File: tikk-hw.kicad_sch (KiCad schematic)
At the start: 18 parts, among them P6 ZX-SH1.0-4PWT, SW1 TS24CA, SW2 TS24CA, U1 IS31FL3731-QFLS2-TR, U2 LIS2DH12TR, U3 ProMicro, U4 CP6208DTR(XBLW), U5 TMP102AIDRLR

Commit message: initial placements all finished
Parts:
- added J1: 51281-0598, 512810598, symbol easyeda2kicad:51281-0598
- added LED10, LED100, LED101, LED102, LED103, LED104, LED105, LED11, LED12, LED13, LED14, LED15, LED16, LED17, LED18, LED19, LED20, LED21, LED22, LED23, LED24, LED25, LED26, LED27, LED28, LED29, LED30, LED31, LED32, LED33, LED34, LED35, LED36, LED37, LED38, LED39, LED40, LED41, LED42, LED43, LED44, LED45, LED46, LED47, LED48, LED49, LED50, LED51, LED52, LED53, LED54, LED55, LED56, LED57, LED58, LED59, LED60, LED61, LED62, LED63, LED64, LED65, LED66, LED67, LED68, LED69, LED70, LED71, LED72, LED73, LED74, LED75, LED76, LED77, LED78, LED79, LED8, LED80, LED81, LED82, LED83, LED84, LED85, LED86, LED87, LED88, LED89, LED9, LED90, LED91, LED92, LED93, LED94, LED95, LED96, LED97, LED98, LED99: F.0402.00003/P2-0402R1TS2-045T-001, easyeda2kicad:LED0402-RD, symbol easyeda2kicad:F.0402.00003_P2-0402R1TS2-045T-001
- added R1, R2: 100K, Resistor_SMD:R_0402_1005Metric, symbol Device:R
- added TP1: NC1, TestPoint:TestPoint_Pad_1.0x1.0mm, symbol Connector:TestPoint
- added TP2: NFC1, TestPoint:TestPoint_Pad_1.0x1.0mm, symbol Connector:TestPoint
- added TP3: NC2, TestPoint:TestPoint_Pad_1.0x1.0mm, symbol Connector:TestPoint
- added TP4: NC3, TestPoint:TestPoint_Pad_1.0x1.0mm, symbol Connector:TestPoint
- added TP5: NFC2, TestPoint:TestPoint_Pad_1.0x1.0mm, symbol Connector:TestPoint
- added TP6: SWCLK, TestPoint:TestPoint_THTPad_1.0x1.0mm_Drill0.5mm, symbol Connector:TestPoint
- added TP7: SWDIO, TestPoint:TestPoint_THTPad_1.0x1.0mm_Drill0.5mm, symbol Connector:TestPoint
- added U6: CP6208DTR(XBLW), easyeda2kicad:SOP-8_L4.9-W3.9-P1.27-LS6.0-BL, symbol easyeda2kicad:CP6208DTR(XBLW)
- U3: value ProMicro -> Tenstar nRF52840; footprint nrfmicro:pro_micro -> nrfmicro:tenstar_nrf52840
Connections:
- net P0.03 is gone; now on net P1.11: U3.10 (1.11)
- net P0.15 is gone; now on net MOTOR2-A: U3.17 (0.17)
- net P0.17 is gone; now on net MOTOR2-B: U3.18 (0.20)
- net P0.28 is gone; now on net P0.10: U3.11 (0.10)
- net P0.31 is gone; now on net P0.29: U3.6 (0.29)
- net P1.06 is gone; now on net SDA: U3.24 (1.06)
- net EXT_VCC: now also U5.5 (V+)
- net GND: now also SW1.3, U5.2 (GND), U5.4 (ADD0), J1.6 (MP1), J1.7 (MP2), R2.2
- net P0.02: now also U3.7 (0.02); no longer U3.8 (PF7)
- net P0.09: now also U3.12 (0.09), J1.5, TP5.1; no longer U3.22 (PE6)
- net P0.10: now also J1.2, TP2.1; no longer U3.23 (PB4)
- net P0.13: now also U3.22 (0.11); no longer U3.20 (PC6)
- net P0.24: now also U3.20 (0.24); no longer U3.21 (PD7)
- net P0.29: no longer U3.7 (PF6)
- net P1.11: no longer U3.12 (PB6)
- net RESET: now also SW1.4
- net VBAT: now also R1.1
- net at U4.2 (Bout): now also H3.3
- net at U4.3 (Aout): now also H3.4
- net MOTOR2-B: now reaches U4.5 (Bin)
- net MOTOR2-A: now reaches U4.8 (Ain)
- net at H3.1: now also U6.2 (Bout)
- net at H3.2: now also U6.3 (Aout)
- net SCL: now reaches U5.1 (SCL)
- net SCL: now also U3.23 (1.04)
- net TMP102_ALERT: now reaches U5.3 (ALERT)
- net SDA: now reaches U5.6 (SDA)
- net P0.06 renamed MOTOR1-A
- net MOTOR1-A: now also U6.8 (Ain)
- net P0.08 renamed MOTOR1-B
- net MOTOR1-B: now also U6.5 (Bin)
- net P0.20 renamed P0.22
- net P0.30 renamed BATTERY-V
- net BATTERY-V: now also R1.2, R2.1
- new net: J1.4, TP4.1
- new net: J1.1, TP1.1
- new net: J1.3, TP3.1
- new net P1.00: U3.21 (1.00)
- new net P1.15: U3.8 (1.15)
- no-connect marks 0 -> 2
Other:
- note added: "Passthrough for programming pads on the tenstar board"
- moved on the sheet: H1, H2, H3, LED1, LED2, LED3, LED4, LED5, LED6, LED7, P6, SW1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

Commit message: added caps
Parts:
- added C10, C11, C12, C8, C9: CC0402KRX7R7BB104, easyeda2kicad:C0402, symbol easyeda2kicad:CC0402KRX7R7BB104
- added C13, C14: CC0603JRNPO8BN561, easyeda2kicad:C0603, symbol easyeda2kicad:CC0603JRNPO8BN561
- added C2: CL21A106KAYNNNE, easyeda2kicad:C0805, symbol easyeda2kicad:CL21A106KAYNNNE
- added C4, C5, C6, C7: CL31A107MQHNNNE, easyeda2kicad:C1206, symbol easyeda2kicad:CL31A107MQHNNNE
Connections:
- net GND: now also SW2.3, C12.1, C13.1, C14.1, C2.1, C4.1, C5.1, C6.1, C7.1, C8.1, C9.1
- net RESET: now also SW2.4
- net at U6.1 (Vcc): now also C4.2, C7.2, C8.2
- net at U6.2 (Bout): now also H3.2; no longer H3.1
- net at U6.3 (Aout): now also H3.1; no longer H3.2
- net at U4.1 (Vcc): now also C5.2, C6.2, C9.2
- net at U4.2 (Bout): now also H3.4; no longer H3.3
- net at U4.3 (Aout): now also H3.3; no longer H3.4
- net at U1.2 (VCC): now also C12.2, C2.2
- net P0.09 renamed NFC1
- net NFC1: now also C14.2
- net P0.10 renamed NFC2
- net NFC2: now also C13.2

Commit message: midway through routing LED matrix
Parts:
- added C1: CL10B224KA8NNNC, easyeda2kicad:C0603, symbol easyeda2kicad:CL10B224KA8NNNC
- added JP1: Jumper_3_Bridged12, Jumper:SolderJumper-3_P1.3mm_Bridged12_Pad1.0x1.5mm_NumberLabels, symbol Jumper:Jumper_3_Bridged12
- added TP8: AUDIO-IN, TestPoint:TestPoint_Pad_D1.0mm, symbol Connector:TestPoint
- renumbered LED7 to LEDC1-R1, LED14 to LEDC1-R2, LED21 to LEDC1-R3, LED28 to LEDC1-R4, LED35 to LEDC1-R5, LED42 to LEDC1-R6, LED49 to LEDC1-R7, LED56 to LEDC1-R8, LED6 to LEDC2-R1, LED13 to LEDC2-R2, LED20 to LEDC2-R3, LED27 to LEDC2-R4, LED34 to LEDC2-R5, LED41 to LEDC2-R6, LED48 to LEDC2-R7, LED55 to LEDC2-R8, LED5 to LEDC3-R1, LED12 to LEDC3-R2, LED19 to LEDC3-R3, LED26 to LEDC3-R4, LED33 to LEDC3-R5, LED40 to LEDC3-R6, LED47 to LEDC3-R7, LED54 to LEDC3-R8, LED4 to LEDC4-R1, LED11 to LEDC4-R2, LED18 to LEDC4-R3, LED25 to LEDC4-R4, LED32 to LEDC4-R5, LED39 to LEDC4-R6, LED46 to LEDC4-R7, LED53 to LEDC4-R8, LED3 to LEDC5-R1, LED10 to LEDC5-R2, LED17 to LEDC5-R3, LED24 to LEDC5-R4, LED31 to LEDC5-R5, LED38 to LEDC5-R6, LED45 to LEDC5-R7, LED52 to LEDC5-R8, LED2 to LEDC6-R1, LED9 to LEDC6-R2, LED16 to LEDC6-R3, LED23 to LEDC6-R4, LED30 to LEDC6-R5, LED37 to LEDC6-R6, LED44 to LEDC6-R7, LED51 to LEDC6-R8, LED1 to LEDC7-R1, LED8 to LEDC7-R2, LED15 to LEDC7-R3, LED22 to LEDC7-R4, LED29 to LEDC7-R5, LED36 to LEDC7-R6, LED43 to LEDC7-R7, LED50 to LEDC7-R8
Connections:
- net EXT_VCC: now also JP1.3 (B)
- net GND: now also U1.5 (GND), U4.4 (GND), U4.7 (GND), U6.4 (GND), U6.7 (GND)
- net SCL: now also U1.20 (SCL)
- net SDA: now also U1.19 (SDA)
- net VBAT: now also JP1.1 (A)
- net CA7: now reaches LEDC7-R7.1 (K)
- net CA7: now also LEDC1-R6.2 (A), LEDC2-R6.2 (A), LEDC3-R6.2 (A), LEDC4-R6.2 (A), LEDC5-R6.2 (A), LEDC6-R6.2 (A), LEDC7-R1.1 (K), LEDC7-R2.1 (K), LEDC7-R3.1 (K), LEDC7-R4.1 (K), LEDC7-R5.1 (K), LEDC7-R6.1 (K), LEDC7-R8.1 (K), U1.27 (CA7)
- net CA8: now reaches LEDC7-R7.2 (A)
- net CA8: now also LEDC1-R7.2 (A), LEDC2-R7.2 (A), LEDC3-R7.2 (A), LEDC4-R7.2 (A), LEDC5-R7.2 (A), LEDC6-R7.2 (A), U1.28 (CA8)
- net CA4: now reaches LEDC4-R8.1 (K)
- net CA4: now also LEDC1-R3.2 (A), LEDC2-R3.2 (A), LEDC3-R3.2 (A), LEDC4-R1.1 (K), LEDC4-R2.1 (K), LEDC4-R3.1 (K), LEDC4-R4.1 (K), LEDC4-R5.1 (K), LEDC4-R6.1 (K), LEDC4-R7.1 (K), LEDC5-R4.2 (A), LEDC6-R4.2 (A), LEDC7-R4.2 (A), U1.24 (CA4)
- net CA9: now reaches LEDC4-R8.2 (A)
- net CA9: now also LEDC1-R8.2 (A), LEDC2-R8.2 (A), LEDC3-R8.2 (A), LEDC5-R8.2 (A), LEDC6-R8.2 (A), LEDC7-R8.2 (A), U1.1 (CA9)
- net CA3: now reaches LEDC3-R8.1 (K)
- net CA3: now also LEDC1-R2.2 (A), LEDC2-R2.2 (A), LEDC3-R1.1 (K), LEDC3-R2.1 (K), LEDC3-R3.1 (K), LEDC3-R4.1 (K), LEDC3-R5.1 (K), LEDC3-R6.1 (K), LEDC3-R7.1 (K), LEDC4-R3.2 (A), LEDC5-R3.2 (A), LEDC6-R3.2 (A), LEDC7-R3.2 (A), U1.23 (CA3)
- net CA1: now reaches LEDC1-R7.1 (K)
- net CA1: now also LEDC1-R1.1 (K), LEDC1-R2.1 (K), LEDC1-R3.1 (K), LEDC1-R4.1 (K), LEDC1-R5.1 (K), LEDC1-R6.1 (K), LEDC1-R8.1 (K), LEDC2-R1.2 (A), LEDC3-R1.2 (A), LEDC4-R1.2 (A), LEDC5-R1.2 (A), LEDC6-R1.2 (A), LEDC7-R1.2 (A), U1.21 (CA1)
- net CA2: now reaches LEDC7-R2.2 (A)
- net CA2: now also LEDC1-R1.2 (A), LEDC2-R1.1 (K), LEDC2-R2.1 (K), LEDC2-R3.1 (K), LEDC2-R4.1 (K), LEDC2-R5.1 (K), LEDC2-R6.1 (K), LEDC2-R7.1 (K), LEDC2-R8.1 (K), LEDC3-R2.2 (A), LEDC4-R2.2 (A), LEDC5-R2.2 (A), LEDC6-R2.2 (A), U1.22 (CA2)
- net CA6: now reaches LEDC3-R5.2 (A)
- net CA6: now also LEDC1-R5.2 (A), LEDC2-R5.2 (A), LEDC4-R5.2 (A), LEDC5-R5.2 (A), LEDC6-R1.1 (K), LEDC6-R2.1 (K), LEDC6-R3.1 (K), LEDC6-R4.1 (K), LEDC6-R5.1 (K), LEDC6-R6.1 (K), LEDC6-R7.1 (K), LEDC6-R8.1 (K), LEDC7-R6.2 (A), U1.26 (CA6)
- net at LED61.2 (A): now also LED60.1 (K)
- net CA5: now reaches LEDC5-R8.1 (K)
- net CA5: now also LEDC1-R4.2 (A), LEDC2-R4.2 (A), LEDC3-R4.2 (A), LEDC4-R4.2 (A), LEDC5-R1.1 (K), LEDC5-R2.1 (K), LEDC5-R3.1 (K), LEDC5-R4.1 (K), LEDC5-R5.1 (K), LEDC5-R6.1 (K), LEDC5-R7.1 (K), LEDC6-R5.2 (A), LEDC7-R5.2 (A), U1.25 (CA5)
- net MOTOR-PWR: now reaches C5.2, C6.2, C9.2, U4.1 (Vcc)
- net MOTOR-PWR: now also C4.2, C7.2, C8.2, U6.1 (Vcc), JP1.2 (C)
- net CB4: now reaches U1.10 (CB4)
- net CB5: now reaches U1.11 (CB5)
- net CB6: now reaches U1.12 (CB6)
- net CB7: now reaches U1.13 (CB7)
- net CB8: now reaches U1.14 (CB8)
- net CB9: now reaches U1.15 (CB9)
- net at U1.17 (IN): now also C1.1
- net LED_SDB: now reaches U1.3 (SDB)
- net LED_INT: now reaches U1.4 (INTB)
- net CB1: now reaches U1.7 (CB1)
- net CB2: now reaches U1.8 (CB2)
- net CB3: now reaches U1.9 (CB3)
- new net: C1.2, TP8.1
- no-connect marks 2 -> 4
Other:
- moved on the sheet: C10, C11, C12, C13, C14, C2, C4, C5, C6, C7, C8, C9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

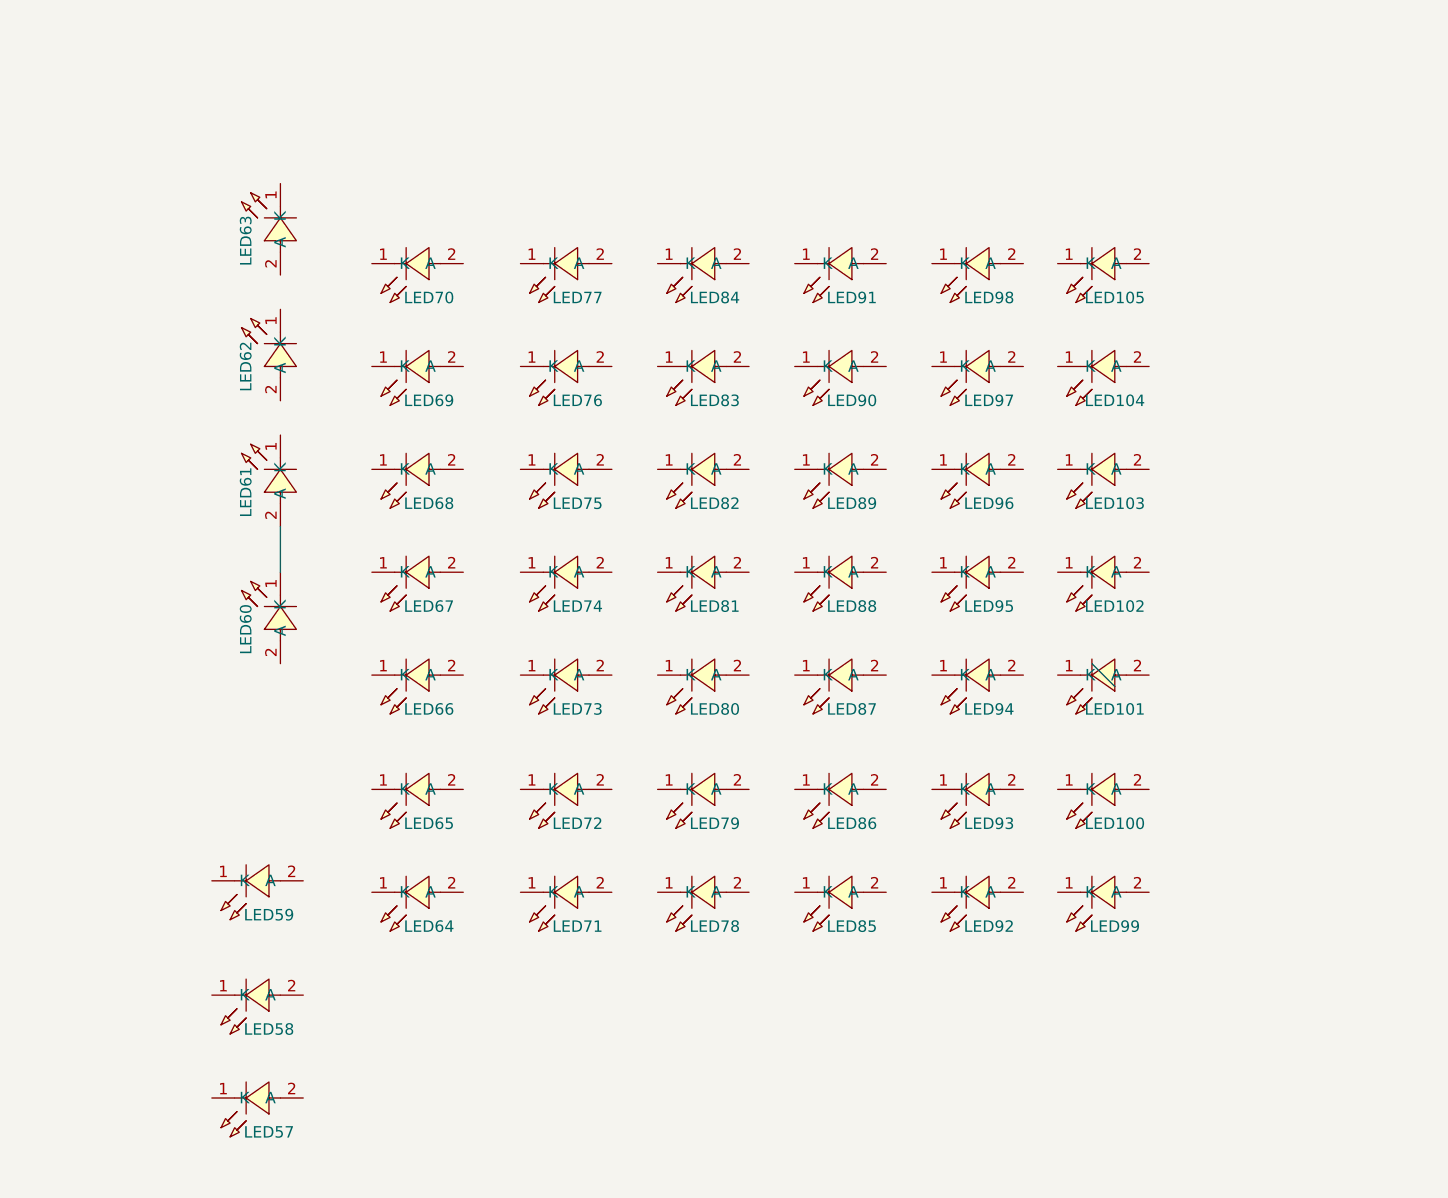
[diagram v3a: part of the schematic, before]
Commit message: all connections to LEDs made on schematics
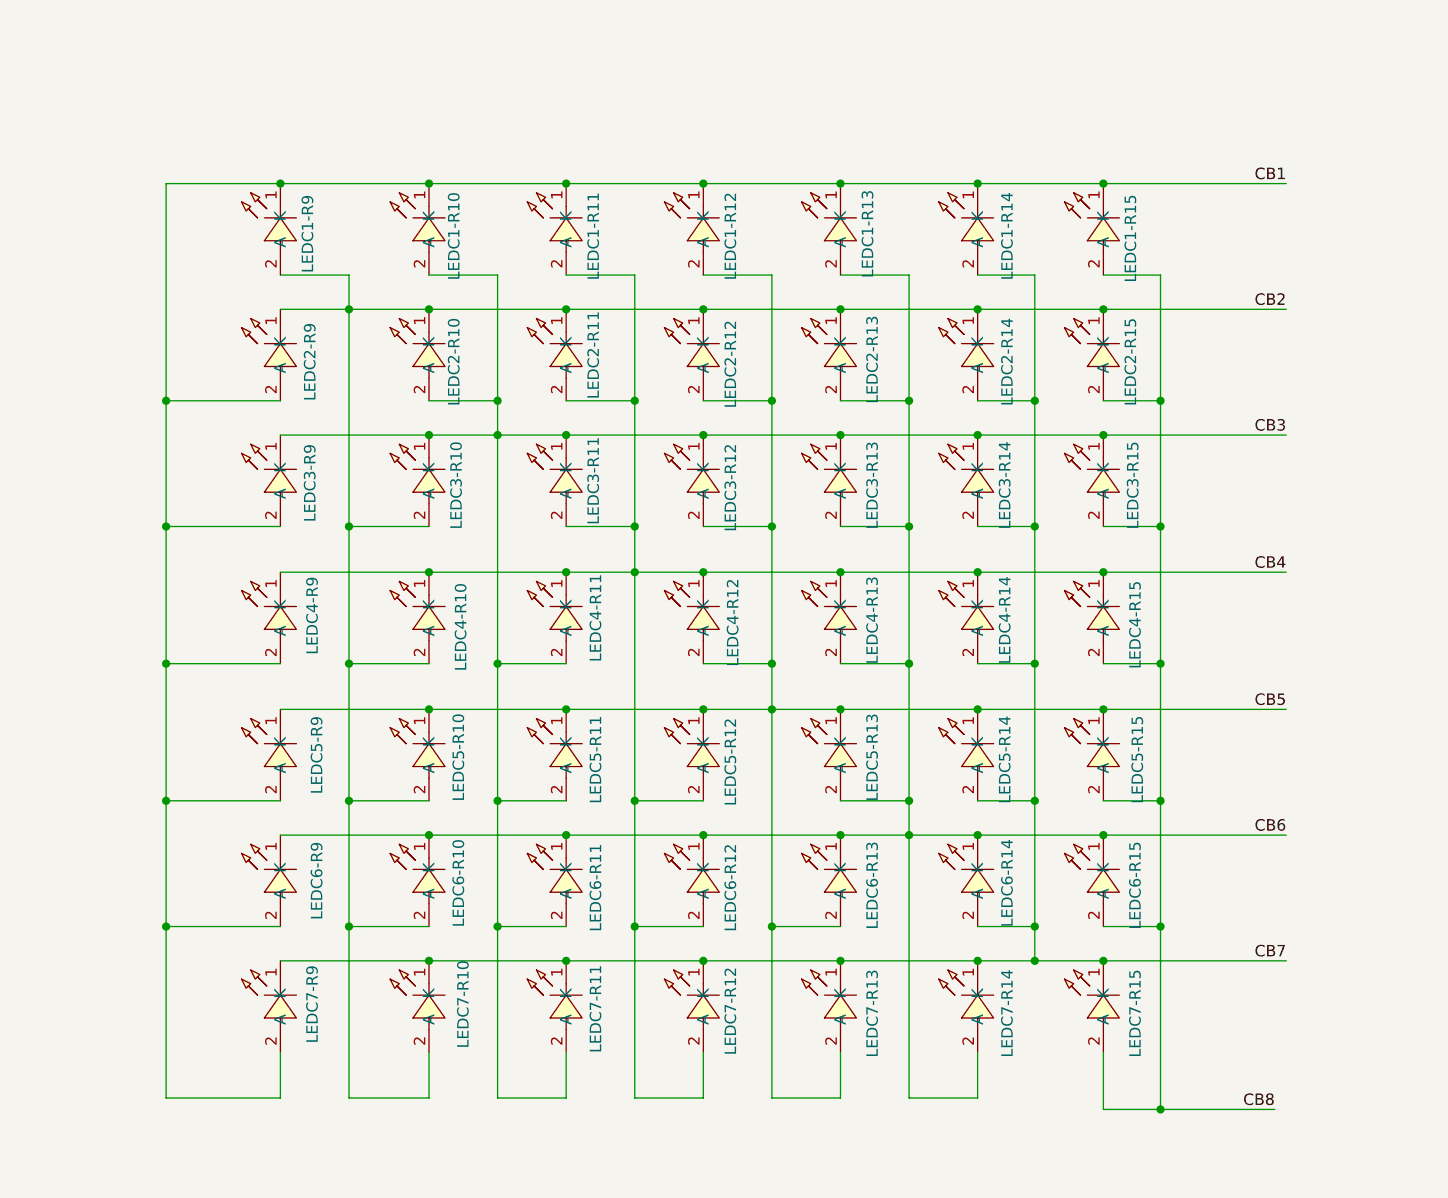
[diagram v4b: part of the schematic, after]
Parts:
- renumbered LED70 to LEDC1-R10, LED77 to LEDC1-R11, LED84 to LEDC1-R12, LED91 to LEDC1-R13, LED98 to LEDC1-R14, LED105 to LEDC1-R15, LED63 to LEDC1-R9, LED69 to LEDC2-R10, LED76 to LEDC2-R11, LED83 to LEDC2-R12, LED90 to LEDC2-R13, LED97 to LEDC2-R14, LED104 to LEDC2-R15, LED62 to LEDC2-R9, LED68 to LEDC3-R10, LED75 to LEDC3-R11, LED82 to LEDC3-R12, LED89 to LEDC3-R13, LED96 to LEDC3-R14, LED103 to LEDC3-R15, LED61 to LEDC3-R9, LED67 to LEDC4-R10, LED74 to LEDC4-R11, LED81 to LEDC4-R12, LED88 to LEDC4-R13, LED95 to LEDC4-R14, LED102 to LEDC4-R15, LED60 to LEDC4-R9, LED66 to LEDC5-R10, LED73 to LEDC5-R11, LED80 to LEDC5-R12, LED87 to LEDC5-R13, LED94 to LEDC5-R14, LED101 to LEDC5-R15, LED59 to LEDC5-R9, LED65 to LEDC6-R10, LED72 to LEDC6-R11, LED79 to LEDC6-R12, LED86 to LEDC6-R13, LED93 to LEDC6-R14, LED100 to LEDC6-R15, LED58 to LEDC6-R9, LED64 to LEDC7-R10, LED71 to LEDC7-R11, LED78 to LEDC7-R12, LED85 to LEDC7-R13, LED92 to LEDC7-R14, LED99 to LEDC7-R15, LED57 to LEDC7-R9
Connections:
- net CB1: now also LEDC1-R10.1 (K), LEDC1-R11.1 (K), LEDC1-R12.1 (K), LEDC1-R13.1 (K), LEDC1-R14.1 (K), LEDC1-R15.1 (K), LEDC1-R9.1 (K), LEDC2-R9.2 (A), LEDC3-R9.2 (A), LEDC4-R9.2 (A), LEDC5-R9.2 (A), LEDC6-R9.2 (A), LEDC7-R9.2 (A)
- net CB2: now also LEDC1-R9.2 (A), LEDC2-R10.1 (K), LEDC2-R11.1 (K), LEDC2-R12.1 (K), LEDC2-R13.1 (K), LEDC2-R14.1 (K), LEDC2-R15.1 (K), LEDC2-R9.1 (K), LEDC3-R10.2 (A), LEDC4-R10.2 (A), LEDC5-R10.2 (A), LEDC6-R10.2 (A), LEDC7-R10.2 (A)
- net CB3: now also LEDC1-R10.2 (A), LEDC2-R10.2 (A), LEDC3-R10.1 (K), LEDC3-R11.1 (K), LEDC3-R12.1 (K), LEDC3-R13.1 (K), LEDC3-R14.1 (K), LEDC3-R15.1 (K), LEDC3-R9.1 (K), LEDC4-R11.2 (A), LEDC5-R11.2 (A), LEDC6-R11.2 (A), LEDC7-R11.2 (A)
- net CB4: now also LEDC1-R11.2 (A), LEDC2-R11.2 (A), LEDC3-R11.2 (A), LEDC4-R10.1 (K), LEDC4-R11.1 (K), LEDC4-R12.1 (K), LEDC4-R13.1 (K), LEDC4-R14.1 (K), LEDC4-R15.1 (K), LEDC4-R9.1 (K), LEDC5-R12.2 (A), LEDC6-R12.2 (A), LEDC7-R12.2 (A)
- net CB5: now also LEDC1-R12.2 (A), LEDC2-R12.2 (A), LEDC3-R12.2 (A), LEDC4-R12.2 (A), LEDC5-R10.1 (K), LEDC5-R11.1 (K), LEDC5-R12.1 (K), LEDC5-R13.1 (K), LEDC5-R14.1 (K), LEDC5-R15.1 (K), LEDC5-R9.1 (K), LEDC6-R13.2 (A), LEDC7-R13.2 (A)
- net CB6: now also LEDC1-R13.2 (A), LEDC2-R13.2 (A), LEDC3-R13.2 (A), LEDC4-R13.2 (A), LEDC5-R13.2 (A), LEDC6-R10.1 (K), LEDC6-R11.1 (K), LEDC6-R12.1 (K), LEDC6-R13.1 (K), LEDC6-R14.1 (K), LEDC6-R15.1 (K), LEDC6-R9.1 (K), LEDC7-R14.2 (A)
- net CB7: now also LEDC1-R14.2 (A), LEDC2-R14.2 (A), LEDC3-R14.2 (A), LEDC4-R14.2 (A), LEDC5-R14.2 (A), LEDC6-R14.2 (A), LEDC7-R10.1 (K), LEDC7-R11.1 (K), LEDC7-R12.1 (K), LEDC7-R13.1 (K), LEDC7-R14.1 (K), LEDC7-R15.1 (K), LEDC7-R9.1 (K)
- net CB8: now also LEDC1-R15.2 (A), LEDC2-R15.2 (A), LEDC3-R15.2 (A), LEDC4-R15.2 (A), LEDC5-R15.2 (A), LEDC6-R15.2 (A), LEDC7-R15.2 (A)
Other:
- moved on the sheet: LEDC1-R10, LEDC1-R11, LEDC1-R12, LEDC1-R13, LEDC1-R14, LEDC1-R15, LEDC2-R10, LEDC2-R11, LEDC2-R12, LEDC2-R13, LEDC2-R14, LEDC2-R15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

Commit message: finished initial layout
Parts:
- added C3: CC0402KRX7R7BB104, easyeda2kicad:C0402, symbol easyeda2kicad:CC0402KRX7R7BB104
- added R3, R4, R5: RC0402FR-0720KL, easyeda2kicad:R0402, symbol easyeda2kicad:RC0402FR-0720KL
- added R6: RC0402FR-07100KL, easyeda2kicad:R0402, symbol easyeda2kicad:RC0402FR-07100KL
- added R7: RC0402FR-070RL, easyeda2kicad:R0402, symbol easyeda2kicad:RC0402FR-070RL
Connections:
- net P0.22 is gone; now on net IMU_INT_2: U3.19 (0.22)
- net P0.24 is gone; now on net IMU_INT_1: U3.20 (0.24)
- net P1.11 is gone; now on net TMP102_ALERT: U3.10 (1.11)
- net EXT_VCC: now also C10.1, C11.1, C12.2, C2.2, P6.3, U1.2 (VCC), U2.10 (VDD_IO), U2.9 (VDD), R4.2, R5.2, R6.1
- net GND: now also C10.2, C11.2, P6.4, P6.5, P6.6, SW1.1, SW1.2, SW2.1, SW2.2, U1.18 (AD), U1.29 (EP), U2.5 (RES), U2.6 (GND), U2.7 (GND), U2.8 (GND), C3.2, R3.1, R7.1
- net RESET: no longer SW1.4
- net SCL: now also P6.1, U2.1 (SCL/SPC), R5.1
- net SDA: now also P6.2, U2.4 (SDA/SDI/SDO), R4.1
- net IMU_INT_2: now reaches U2.11 (INT2)
- net IMU_INT_1: now reaches U2.12 (INT1)
- net at U2.2 (CS): now also R6.2
- net at U2.3 (SDO/SA0): now also R7.2
- net at U1.16 (C_FILT): now also C3.1
- net at U1.6 (R-EXT): now also R3.2
- net P0.13 renamed USER
- net USER: now also SW1.4
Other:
- note added: "Accelerometer"
- note added: "Buttons"
- note added: "LED Driver"
- note added: "Motor Drivers"
- note added: "NFC Connector"
- note added: "ProMicro Header"
- note added: "QWIIC Connector"
- note added: "Temp Sensor"
- moved on the sheet: C1, C10, C11, C12, C13, C14, C2, C4, C5, C6, C7, C8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
